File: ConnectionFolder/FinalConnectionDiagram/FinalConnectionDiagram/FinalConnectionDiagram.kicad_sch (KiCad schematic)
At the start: 0 parts

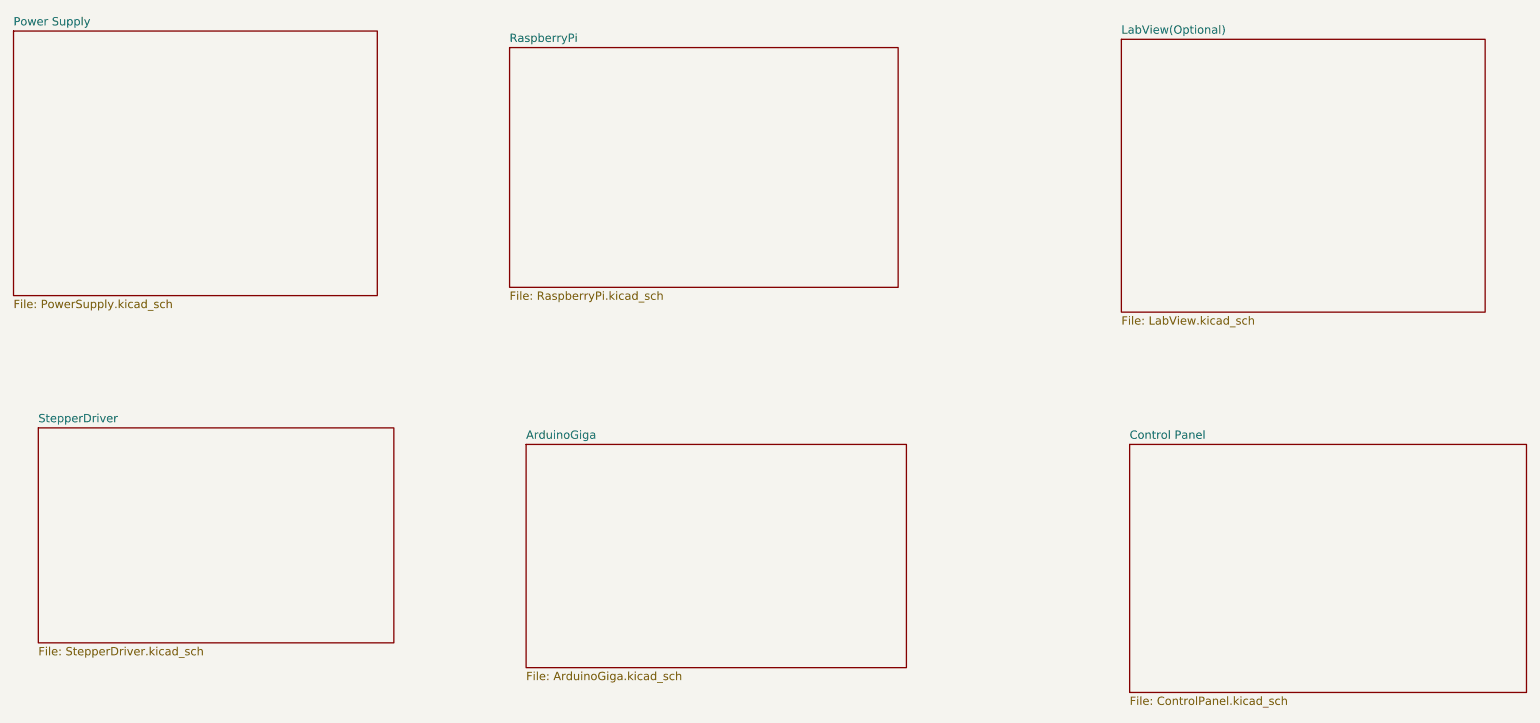
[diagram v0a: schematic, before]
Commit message: KiCad schematic updated.
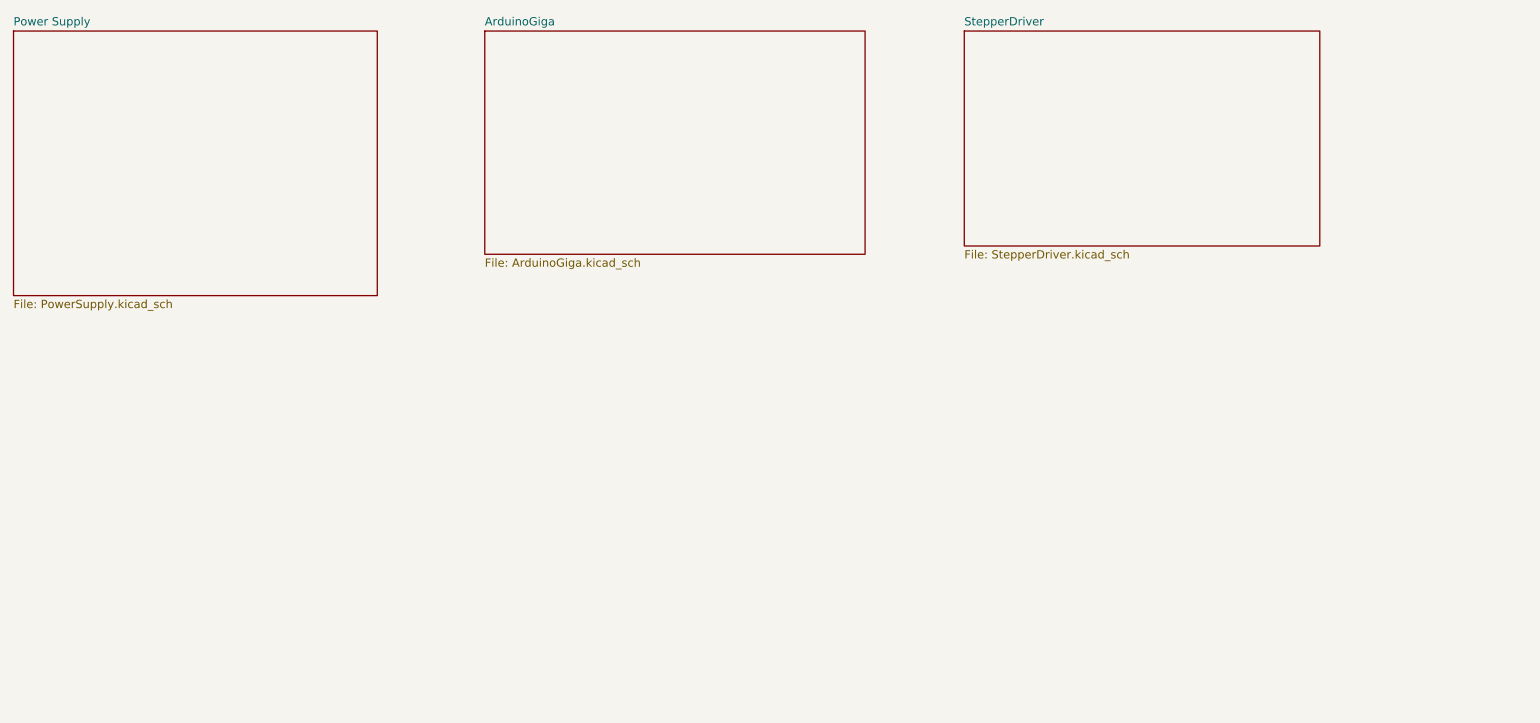
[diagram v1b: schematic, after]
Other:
- removed sheet Control Panel
- removed sheet LabView(Optional)
- removed sheet RaspberryPi
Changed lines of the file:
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@@
 	)
 	(sheet
-		(at 27.94 87.63)
+		(at 170.18 26.67)
 		(size 54.61 33.02)
 		(exclude_from_sim no)
@@
 		)
 		(property "Sheetname" "StepperDriver"
-			(at 27.94 86.9184 0)
+			(at 170.18 25.9584 0)
 			(effects
 				(font
@@
 		)
 		(property "Sheetfile" "StepperDriver.kicad_sch"
-			(at 27.94 121.2346 0)
+			(at 170.18 60.2746 0)
 			(effects
 				(font
@@
 	)
 	(sheet
-		(at 195.58 90.17)
-		(size 60.96 38.1)
-		(exclude_from_sim no)
-		(in_bom yes)
-		(on_board yes)
-		(dnp no)
-		(fields_autoplaced yes)
-		(stroke
-			(width 0.1524)
-			(type solid)
-		)
-		(fill
-			(color 0 0 0 0.0000)
-		)
-		(property "Sheetname" "Control Panel"
-			(at 195.58 89.4584 0)
-			(effects
-				(font
-					(size 1.27 1.27)
-				)
-				(justify left bottom)
-			)
-		)
-		(property "Sheetfile" "ControlPanel.kicad_sch"
-			(at 195.58 128.8546 0)
-			(effects
-				(font
-					(size 1.27 1.27)
-				)
-				(justify left top)
-			)
-		)
-		(instances
-			(project "FinalConnectionDiagram"
-				(path "/3cb2e715-dcdc-40c0-b9df-54068ea48efd"
-					(page "6")
-				)
-			)
-		)
-	)
-	(sheet
-		(at 100.33 29.21)
-		(size 59.69 36.83)
-		(exclude_from_sim no)
-		(in_bom yes)
-		(on_board yes)
-		(dnp no)
-		(fields_autoplaced yes)
-		(stroke
-			(width 0.1524)
-			(type solid)
-		)
-		(fill
-			(color 0 0 0 0.0000)
-		)
-		(property "Sheetname" "RaspberryPi"
-			(at 100.33 28.4984 0)
-			(effects
-				(font
-					(size 1.27 1.27)
-				)
-				(justify left bottom)
-			)
-		)
-		(property "Sheetfile" "RaspberryPi.kicad_sch"
-			(at 100.33 66.6246 0)
-			(effects
-				(font
-					(size 1.27 1.27)
-				)
-				(justify left top)
-			)
-		)
-		(instances
-			(project "FinalConnectionDiagram"
-				(path "/3cb2e715-dcdc-40c0-b9df-54068ea48efd"
-					(page "3")
-				)
-			)
-		)
-	)
-	(sheet
-		(at 194.31 27.94)
-		(size 55.88 41.91)
-		(exclude_from_sim no)
-		(in_bom yes)
-		(on_board yes)
-		(dnp no)
-		(fields_autoplaced yes)
-		(stroke
-			(width 0.1524)
-			(type solid)
-		)
-		(fill
-			(color 0 0 0 0.0000)
-		)
-		(property "Sheetname" "LabView(Optional)"
-			(at 194.31 27.2284 0)
-			(effects
-				(font
-					(size 1.27 1.27)
-				)
-				(justify left bottom)
-			)
-		)
-		(property "Sheetfile" "LabView.kicad_sch"
-			(at 194.31 70.4346 0)
-			(effects
-				(font
-					(size 1.27 1.27)
-				)
-				(justify left top)
-			)
-		)
-		(instances
-			(project "FinalConnectionDiagram"
-				(path "/3cb2e715-dcdc-40c0-b9df-54068ea48efd"
-					(page "5")
-				)
-			)
-		)
-	)
-	(sheet
-		(at 102.87 90.17)
+		(at 96.52 26.67)
 		(size 58.42 34.29)
 		(exclude_from_sim no)
@@
 		)
 		(property "Sheetname" "ArduinoGiga"
-			(at 102.87 89.4584 0)
+			(at 96.52 25.9584 0)
 			(effects
 				(font
@@
 		)
 		(property "Sheetfile" "ArduinoGiga.kicad_sch"
-			(at 102.87 125.0446 0)
+			(at 96.52 61.5446 0)
 			(effects
 				(font
